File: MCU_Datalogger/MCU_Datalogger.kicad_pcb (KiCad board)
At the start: 2 copper layers, 29 parts, among them J1 Conn_01x09_Pin, J2 Conn_01x04_Pin, J3 Conn_01x04_Pin, J4 Conn_02x03_Odd_Even, U1 24LC1025, U2 24LC1025, U3 DS1337S_, U4 ATMEGA328P-AU, Y1 32.768 KHz, Y2 16MHz

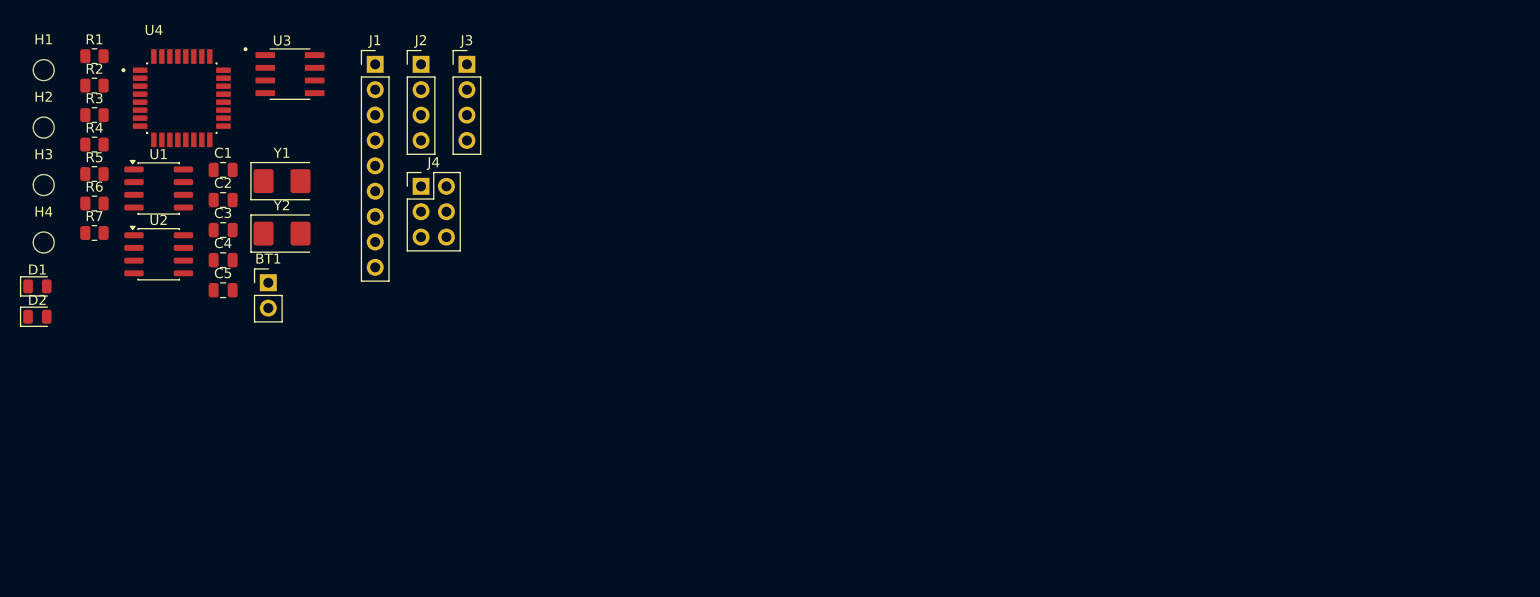
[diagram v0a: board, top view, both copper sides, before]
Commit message: Finshed MCU_Datalogger 2 layer PCB Design and Layout
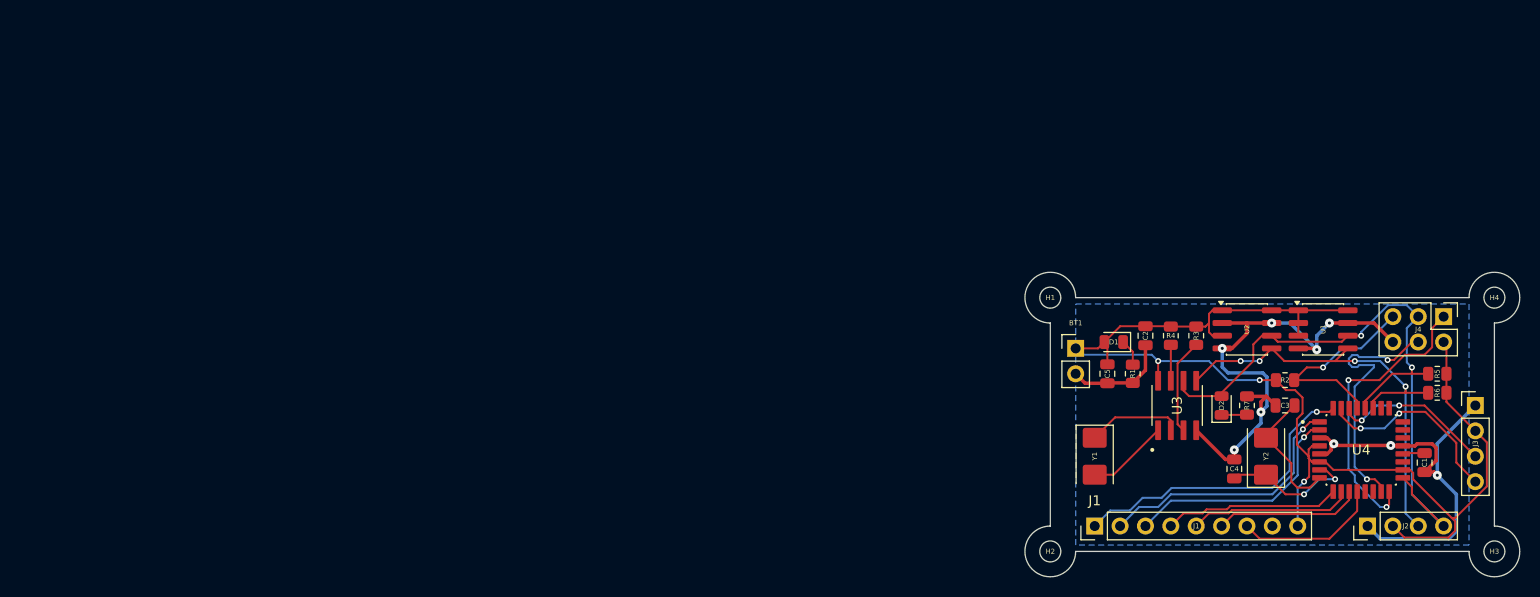
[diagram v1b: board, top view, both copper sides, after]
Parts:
- moved H3 149.8 mm to (175.3, 78.7)
- moved H4 145.3 mm to (175.3, 53.3)
- moved R5 135.9 mm to (169.5, 61.0), turned to 180 degrees
- moved R6 135.7 mm to (169.5, 62.9), turned to 180 degrees
- moved C1 123.8 mm to (168.3, 69.8), turned to -90 degrees
- moved U4 123.2 mm to (161.9, 68.6)
- moved R2 122.8 mm to (154.3, 61.6), turned to 180 degrees
- moved D2 118.9 mm to (148.0, 64.1), turned to 90 degrees
- moved U1 117.4 mm to (158.1, 56.5)
- moved R7 116.6 mm to (150.5, 64.1), turned to 90 degrees
- moved R3 112.5 mm to (145.4, 57.1), turned to -90 degrees
- moved R4 109.4 mm to (142.9, 57.1), turned to -90 degrees
- moved H2 109.3 mm to (130.8, 78.7)
- moved U2 109.2 mm to (150.5, 56.5)
- moved R1 108.7 mm to (139.1, 61.0), turned to -90 degrees
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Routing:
- net VCC: track 0.00 -> 126.0 mm, vias 0 -> 3
- net GND: track 0.00 -> 107.1 mm, vias 0 -> 9
- net /SCK: track 0.00 -> 69.8 mm, vias 0 -> 2
- net /SDA: track 0.00 -> 47.4 mm, vias 0 -> 4
- net /D2: track 0.00 -> 30.9 mm, vias 0 -> 1
- net /MISO: track 0.00 -> 29.6 mm, vias 0 -> 2
- net /D3: track 0.00 -> 26.3 mm, vias 0 -> 1
- net /MOSI: track 0.00 -> 26.3 mm, vias 0 -> 2
- net /D4: track 0.00 -> 23.3 mm, vias 0 -> 1
- net /RESET: track 0.00 -> 20.4 mm, vias 0 -> 1
- net /TX: track 0.00 -> 19.4 mm, vias 0 -> 2
- net /D5: track 0.00 -> 17.7 mm
- net /D6: track 0.00 -> 16.4 mm
- net /RX: track 0.00 -> 16.2 mm, vias 0 -> 2
- net /D7: track 0.00 -> 14.7 mm
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- added copper zone on B.Cu, net GND
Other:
- board outline added: 49.5 x 30.5 mm
